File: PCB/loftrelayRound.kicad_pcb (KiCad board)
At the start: 2 copper layers, 70.1 x 70.1 mm, 29 parts, among them J1 PowerIn, J2 Load, J3 SenSor, J4 Program, K1 G5Q-14-EU DC5, Q1 2N7002, U1 AP1117-33, U2 PC817, U4 ESP-12E

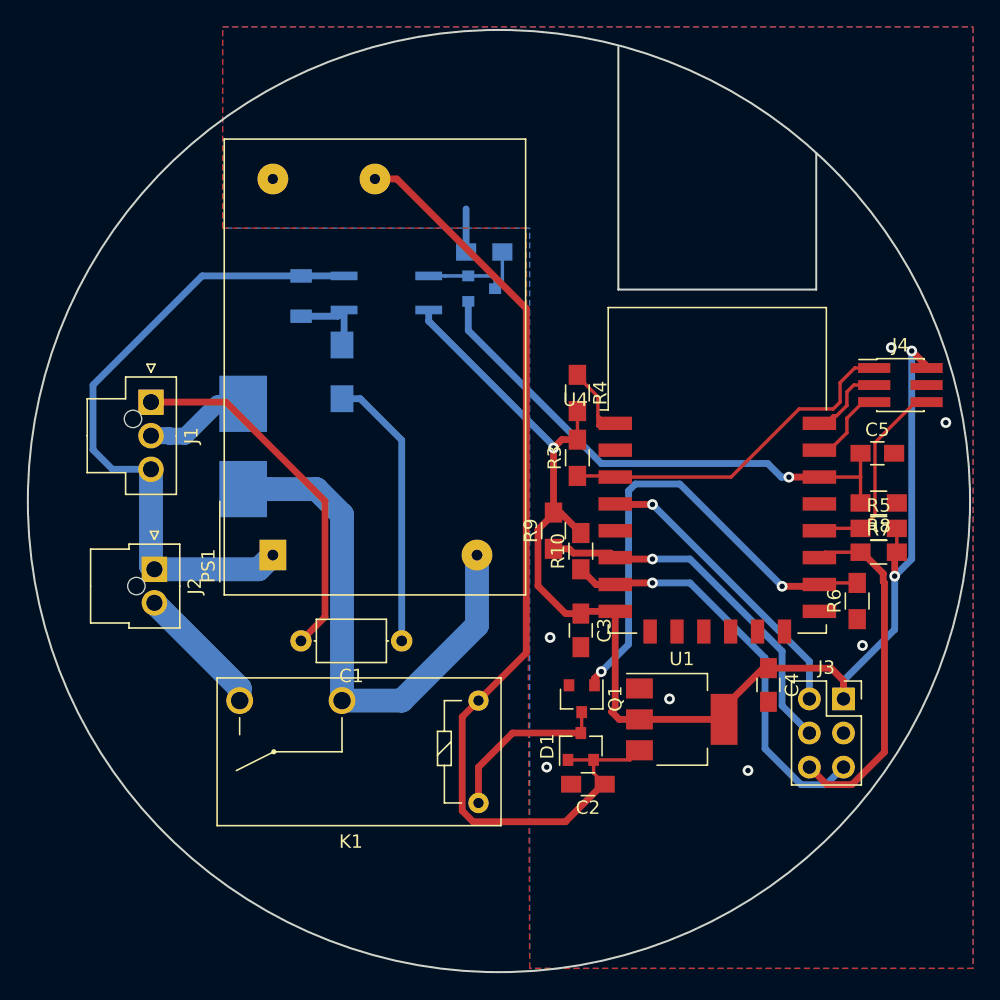
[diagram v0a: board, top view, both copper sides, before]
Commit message: Ændret stik
Har ændret til til 3mm mikrofit fjernet C ved optocobler for at undgå stød.
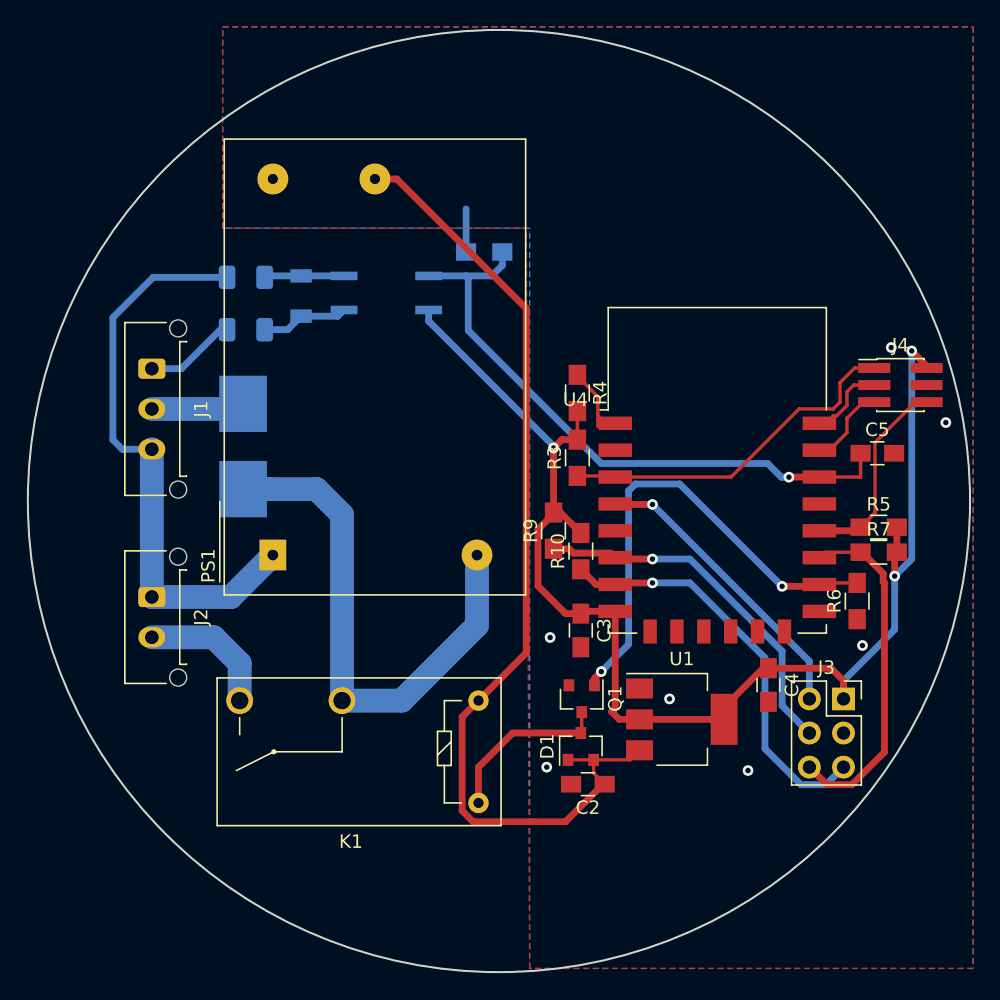
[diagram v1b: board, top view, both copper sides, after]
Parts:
- removed C1: 33nF, Capacitors_THT:C_Axial_L5.1mm_D3.1mm_P7.50mm_Horizontal
- removed D3: BAT54A, Package_TO_SOT_SMD:SOT-23
- C5: value 100nF -> 1uF
- J1: footprint Connectors_Molex:Molex_NanoFit_1x03x2.50mm_Straight -> Connector_Molex:Molex_Micro-Fit_3.0_43650-0315_1x03_P3.00mm_Vertical
- J2: footprint Connectors_Molex:Molex_NanoFit_1x02x2.50mm_Straight -> Connector_Molex:Molex_Micro-Fit_3.0_43650-0215_1x02_P3.00mm_Vertical
- R1: value 100R -> 10k; footprint Resistors_SMD:R_1206_HandSoldering -> Resistor_SMD:R_1206_3216Metric
- R8: footprint Resistors_SMD:R_0805_HandSoldering -> Resistor_SMD:R_1206_3216Metric; moved to B.Cu
- moved R8 50.0 mm to (130.0, 101.2)
- moved R1 7.82 mm to (130.0, 105.1), turned to 180 degrees
- moved J1 2.49 mm to (123.0, 108.0)
- moved J2 2.07 mm to (123.0, 125.0)
- moved R5 0.09 mm to (177.1, 119.8)
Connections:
- J1 pad 1: Net-(C1-Pad2) -> Net-(J1-Pad1)
- J1 pad 3: Net-(D2-Pad2) -> Net-(J1-Pad3)
- J2 pad 1: Net-(D2-Pad2) -> Net-(J1-Pad3)
- PS1 pad 1: Net-(D2-Pad2) -> Net-(J1-Pad3)
- R1 pad 2: Net-(C1-Pad1) -> Net-(J1-Pad1)
- R2 pad 2: Net-(D3-Pad2) -> /Opto
- R8 pad 1: GNDD -> Net-(D2-Pad2)
- R8 pad 2: /Opto -> Net-(J1-Pad3)
- U2 pad 3: Net-(D3-Pad2) -> /Opto
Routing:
- net Net-(J1-Pad3): track 0.00 -> 43.3 mm
- net Net-(D2-Pad2): track 48.6 -> 5.96 mm
- net Net-(C1-Pad2): track 27.2 -> 0.00 mm
- net Net-(C1-Pad1): track 20.7 -> 0.00 mm
- net Net-(D3-Pad2): track 8.67 -> 0.00 mm
- net /Opto: track 40.2 -> 47.0 mm
- net Net-(J1-Pad1): track 0.00 -> 6.80 mm
- net Net-(F1-Pad2): track 7.87 -> 6.95 mm
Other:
- outline, holes or cut-outs redrawn

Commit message: Update af komponeter samt ny programmer
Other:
- outline, holes or cut-outs redrawn
